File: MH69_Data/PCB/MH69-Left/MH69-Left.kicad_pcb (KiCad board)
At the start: 2 copper layers, 163.2 x 92 mm, 78 parts, among them U1 nice_nano

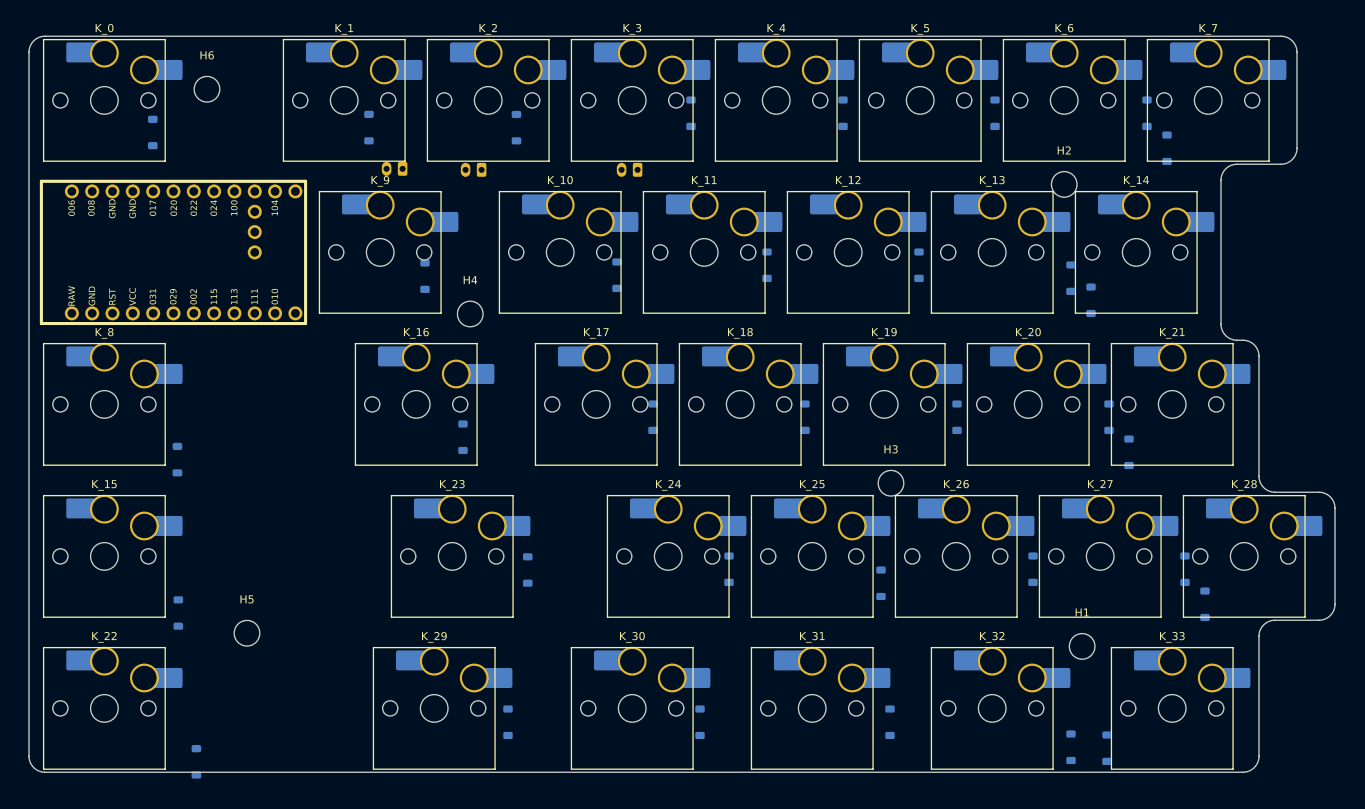
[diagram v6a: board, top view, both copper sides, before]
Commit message: fine touches on edge cuts mostly
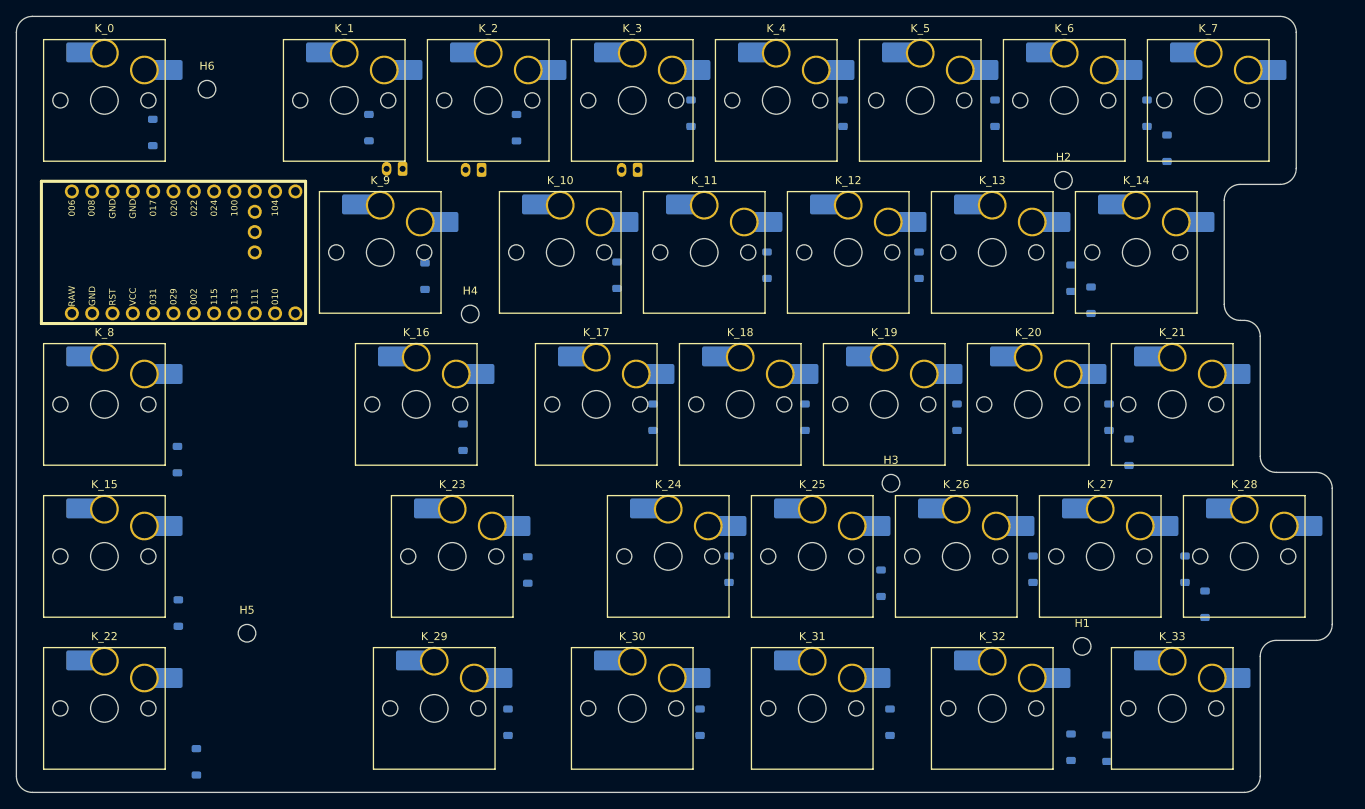
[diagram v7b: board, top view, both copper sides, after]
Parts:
- H1, H2, H3, H4, H5, H6: footprint MountingHole:MountingHole_3.2mm_M3 -> MountingHole:MountingHole_2.2mm_M2_DIN965
- moved H2 0.52 mm to (161.7, 71.8)
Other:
- board size 163.2 x 92 mm -> 164.5 x 97 mm

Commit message: Updated some libs
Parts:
- removed H3: MountingHole, MountingHole:MountingHole_2.2mm_M2_DIN965
- H1, H2, H4, H5, H6: footprint MountingHole:MountingHole_2.2mm_M2_DIN965 -> ScottoKeebs_Scotto:Standoff_M2x6mm
- moved H5 16.2 mm to (56.6, 144.3)
- moved H1 13.1 mm to (164.1, 143.1)
- moved H4 12.5 mm to (92.2, 100.0)
- moved D_33 11.2 mm to (178.3, 142.3)
- moved D_32 6.72 mm to (155.9, 141.9)
- moved H6 6.08 mm to (56.6, 54.6)
